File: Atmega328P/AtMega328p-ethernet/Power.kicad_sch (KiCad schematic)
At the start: 3 parts, among them U4 NCP1117-3.3_SOT223

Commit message: Added lots of lcsc part numbers
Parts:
- C28, C29: LCSC (none) -> C13585
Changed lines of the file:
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@@
+			)
+		)
+		(property "LCSC" "C13585"
+			(at 125.73 85.09 0)
+			(effects
+				(font
+					(size 1.27 1.27)
+				)
+				(hide yes)
 			)
 		)
@@
 			(at 154.94 85.09 0)
 			(effects
+				(font
+					(size 1.27 1.27)
+				)
+				(hide yes)
+			)
+		)
+		(property "LCSC" "C13585"
+			(at 154.94 85.09 0)
+			(effects

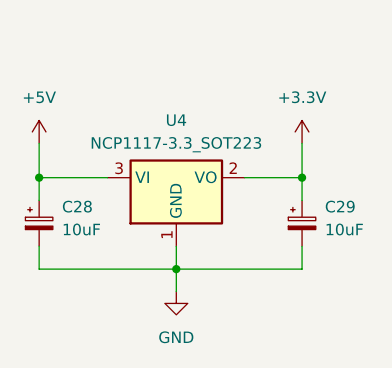
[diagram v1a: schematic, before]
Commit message: Most components selected using lcsc
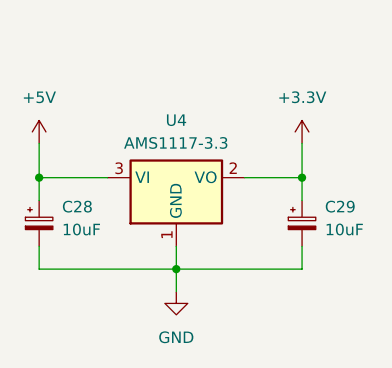
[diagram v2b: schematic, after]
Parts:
- removed U4: NCP1117-3.3_SOT223, Package_TO_SOT_SMD:SOT-223-3_TabPin2, symbol Regulator_Linear:NCP1117-3.3_SOT223
- added U4: AMS1117-3.3, Package_TO_SOT_SMD:SOT-223-3_TabPin2, symbol Regulator_Linear:AMS1117-3.3
- C28, C29: footprint Capacitor_SMD:CP_Elec_4x3 -> Capacitor_SMD:C_1206_3216Metric
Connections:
- net +3.3V: now also U4.2 (VO)
- net +5V: now also U4.3 (VI)
- net GND: now also U4.1 (GND)
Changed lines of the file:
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@@
 			)
 		)
-		(property "Footprint" "Capacitor_SMD:CP_Elec_4x3"
+		(property "Footprint" "Capacitor_SMD:C_1206_3216Metric"
 			(at 125.73 85.09 0)
 			(effects
@@
 				(path "/441f74dc-335f-4227-aefc-792ec34889a2/067fa411-eb49-4894-a2bc-fd168ded14ca"
 					(reference "C28")
-					(unit 1)
-				)
-			)
-		)
-	)
-	(symbol
-		(lib_id "Regulator_Linear:NCP1117-3.3_SOT223")
-		(at 140.97 80.01 0)
-		(unit 1)
-		(exclude_from_sim no)
-		(in_bom yes)
-		(on_board yes)
-		(dnp no)
-		(fields_autoplaced yes)
-		(property "Reference" "U4"
-			(at 140.97 73.66 0)
-			(effects
-				(font
-					(size 1.27 1.27)
-				)
-			)
-		)
-		(property "Value" "NCP1117-3.3_SOT223"
-			(at 140.97 76.2 0)
-			(effects
-				(font
-					(size 1.27 1.27)
-				)
-			)
-		)
-		(property "Footprint" "Package_TO_SOT_SMD:SOT-223-3_TabPin2"
-			(at 140.97 74.93 0)
-			(effects
-				(font
-					(size 1.27 1.27)
-				)
-				(hide yes)
-			)
-		)
-		(property "Datasheet" "http://www.onsemi.com/pub_link/Collateral/NCP1117-D.PDF"
-			(at 143.51 86.36 0)
-			(effects
-				(font
-					(size 1.27 1.27)
-				)
-				(hide yes)
-			)
-		)
-		(property "Description" "1A Low drop-out regulator, Fixed Output 3.3V, SOT-223"
-			(at 140.97 80.01 0)
-			(effects
-				(font
-					(size 1.27 1.27)
-				)
-				(hide yes)
-			)
-		)
-		(pin "3"
-		)
-		(pin "1"
-		)
-		(pin "2"
-		)
-		(instances
-			(project ""
-				(path "/441f74dc-335f-4227-aefc-792ec34889a2/067fa411-eb49-4894-a2bc-fd168ded14ca"
-					(reference "U4")
 					(unit 1)
 				)
@@
 			)
 		)
-		(property "Footprint" "Capacitor_SMD:CP_Elec_4x3"
+		(property "Footprint" "Capacitor_SMD:C_1206_3216Metric"
 			(at 154.94 85.09 0)
 			(effects
@@
 					(unit 1)
 				)
+			)
+		)
+	)
+	(symbol
+		(lib_id "Regulator_Linear:AMS1117-3.3")
+		(at 140.97 80.01 0)
+		(unit 1)
+		(exclude_from_sim no)
+		(in_bom yes)
+		(on_board yes)
+		(dnp no)
+		(fields_autoplaced yes)
+		(property "Reference" "U4"
+			(at 140.97 73.66 0)
+			(effects
+				(font
+					(size 1.27 1.27)
+				)
+			)
+		)
+		(property "Value" "AMS1117-3.3"
+			(at 140.97 76.2 0)
+			(effects
+				(font
+					(size 1.27 1.27)
+				)
+			)
+		)
+		(property "Footprint" "Package_TO_SOT_SMD:SOT-223-3_TabPin2"
+			(at 140.97 74.93 0)
+			(effects
+				(font
+					(size 1.27 1.27)
+				)
+				(hide yes)
+			)
+		)
+		(property "Datasheet" "http://www.advanced-monolithic.com/pdf/ds1117.pdf"
+			(at 143.51 86.36 0)
+			(effects
+				(font
+					(size 1.27 1.27)
+				)
+				(hide yes)
+			)
+		)
+		(property "Description" "1A Low Dropout regulator, positive, 3.3V fixed output, SOT-223"
+			(at 140.97 80.01 0)
+			(effects
+				(font
+					(size 1.27 1.27)
+				)
+				(hide yes)
+			)
+		)
+		(property "LCSC" "C6186"
+			(at 140.97 80.01 0)
+			(effects
+				(font
+					(size 1.27 1.27)
+				)
+				(hide yes)
+			)
+		)
+		(pin "2"
+		)
+		(pin "3"
+		)
+		(pin "1"
+		)
+		(instances
+			(project ""
+				(path "/441f74dc-335f-4227-aefc-792ec34889a2/067fa411-eb49-4894-a2bc-fd168ded14ca"
+					(reference "U4")
+					(unit 1)
+				)

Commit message: Continued cleanup
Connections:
- net +3.3V renamed +3.3V_OUT
- net +5V renamed +5V_IN
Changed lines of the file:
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@@
+		)
+	)
+	(hierarchical_label "+5V_IN"
+		(shape input)
+		(at 125.73 76.2 90)
+		(effects
+			(font
+				(size 1.27 1.27)
+			)
+			(justify left)
+		)
+	)
+	(hierarchical_label "+3.3V_OUT"
+		(shape output)
+		(at 154.94 76.2 90)
+		(effects
+			(font
+				(size 1.27 1.27)
+			)
+			(justify left)
 		)
 	)
@@
 	)
 	(symbol
-		(lib_id "power:+3.3V")
-		(at 154.94 76.2 0)
-		(unit 1)
-		(exclude_from_sim no)
-		(in_bom yes)
-		(on_board yes)
-		(dnp no)
-		(fields_autoplaced yes)
-		(property "Reference" "#PWR046"
-			(at 154.94 80.01 0)
-			(effects
-				(font
-					(size 1.27 1.27)
-				)
-				(hide yes)
-			)
-		)
-		(property "Value" "+3.3V"
-			(at 154.94 71.12 0)
-			(effects
-				(font
-					(size 1.27 1.27)
-				)
-			)
-		)
-		(property "Footprint" ""
-			(at 154.94 76.2 0)
-			(effects
-				(font
-					(size 1.27 1.27)
-				)
-				(hide yes)
-			)
-		)
-		(property "Datasheet" ""
-			(at 154.94 76.2 0)
-			(effects
-				(font
-					(size 1.27 1.27)
-				)
-				(hide yes)
-			)
-		)
-		(property "Description" "Power symbol creates a global label with name \"+3.3V\""
-			(at 154.94 76.2 0)
-			(effects
-				(font
-					(size 1.27 1.27)
-				)
-				(hide yes)
-			)
-		)
-		(pin "1"
-		)
-		(instances
-			(project ""
-				(path "/441f74dc-335f-4227-aefc-792ec34889a2/067fa411-eb49-4894-a2bc-fd168ded14ca"
-					(reference "#PWR046")
-					(unit 1)
-				)
-			)
-		)
-	)
-	(symbol
 		(lib_id "Regulator_Linear:AMS1117-3.3")
 		(at 140.97 80.01 0)
@@
 					(unit 1)
 				)
-			)
-		)
-	)
-	(symbol
-		(lib_id "power:+5V")
-		(at 125.73 76.2 0)
-		(unit 1)
-		(exclude_from_sim no)
-		(in_bom yes)
-		(on_board yes)
-		(dnp no)
-		(fields_autoplaced yes)
-		(property "Reference" "#PWR047"
-			(at 125.73 80.01 0)
-			(effects
-				(font
-					(size 1.27 1.27)
-				)
-				(hide yes)
-			)
-		)
-		(property "Value" "+5V"
-			(at 125.73 71.12 0)
-			(effects
-				(font
-					(size 1.27 1.27)
-				)
-			)
-		)
-		(property "Footprint" ""
-			(at 125.73 76.2 0)
-			(effects
-				(font
-					(size 1.27 1.27)
-				)
-				(hide yes)
-			)
-		)
-		(property "Datasheet" ""
-			(at 125.73 76.2 0)
-			(effects
-				(font
-					(size 1.27 1.27)
-				)
-				(hide yes)
-			)
-		)
-		(property "Description" "Power symbol creates a global label with name \"+5V\""
-			(at 125.73 76.2 0)
-			(effects
-				(font
-					(size 1.27 1.27)
-				)
-				(hide yes)
-			)
-		)
-		(pin "1"
-		)
-		(instances
-			(project ""
-				(path "/441f74dc-335f-4227-aefc-792ec34889a2/067fa411-eb49-4894-a2bc-fd168ded14ca"
-					(reference "#PWR047")
-					(unit 1)
-				)
